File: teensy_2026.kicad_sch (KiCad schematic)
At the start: 12 parts, among them J1 LED, J15 LinAct1, J2 BattManagement, J3 LinearActSaber, J5 LinAct2, U1 RASPBERRY_PI_PICO

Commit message: Merge FIx uo
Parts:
- J15: footprint teensy:4pinJST -> Connector:Tag-Connect_TC2030-IDC-FP_2x03_P1.27mm_Vertical
- J5: footprint teensy:4pinJST -> (none)
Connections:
- net GND: now also J15.4 (Pin_4), J5.4 (Pin_4)
- net LA1_HE1_in: now also J15.1 (Pin_1)
- net LA1_HE2_in: now also J15.2 (Pin_2)
- net LA2_HE1_in: now also J5.1 (Pin_1)
- net LinAct TX: now reaches J3.2 (Pin_2), TP10.1
- new net LA2_HE2_in: J5.2 (Pin_2)
- new net VCC: J15.3 (Pin_3), J5.3 (Pin_3)
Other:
- moved on the sheet: J1, J2, J3, TP10, TP9

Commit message: some small movements
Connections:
- net BattManagement CSn: now also U1.GP1
- net BattManagement TX: now also U1.GP3
- net LA1_HE1_in: now also U1.GP6
- net LA2_HE2_in: now also U1.GP9
- net SCL 0: now also U1.GP19
- no-connect marks 0 -> 17

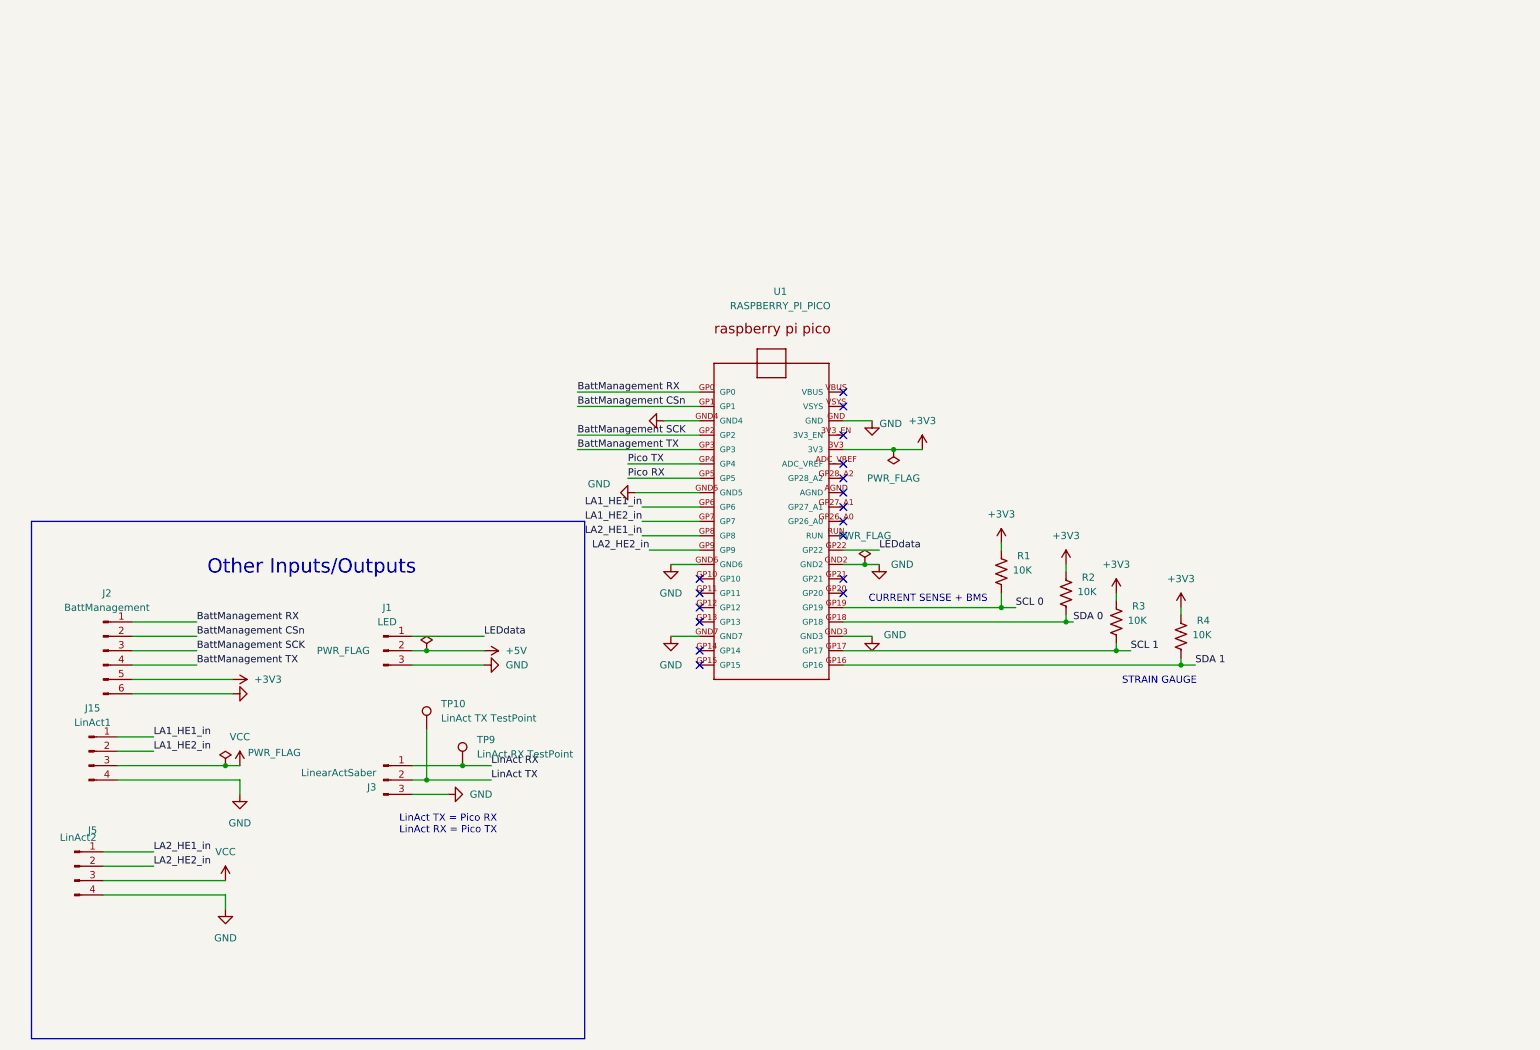
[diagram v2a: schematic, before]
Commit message: Added 3 JSTs for current sense, and 5 JSTs for strain gauge
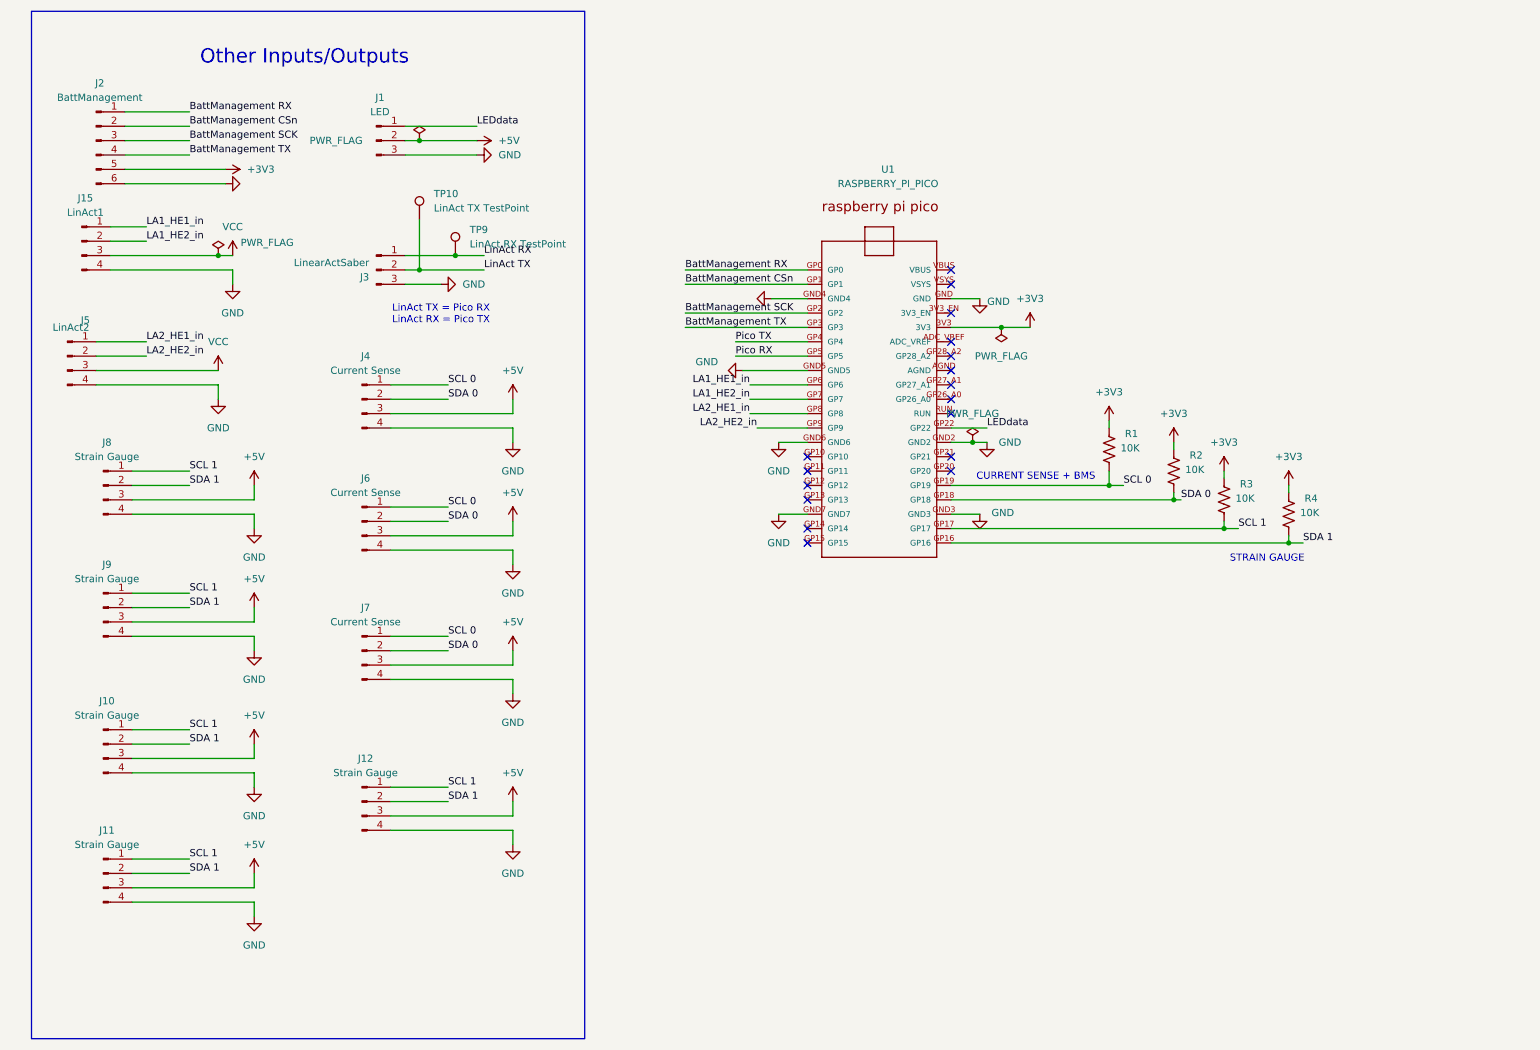
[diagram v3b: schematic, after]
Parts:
- added J10, J11, J12, J8, J9: Strain Gauge, symbol Connector:Conn_01x04_Pin
- added J4, J6, J7: Current Sense, symbol Connector:Conn_01x04_Pin
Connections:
- net +5V: now also J10.3 (Pin_3), J11.3 (Pin_3), J12.3 (Pin_3), J4.3 (Pin_3), J6.3 (Pin_3), J7.3 (Pin_3), J8.3 (Pin_3), J9.3 (Pin_3)
- net GND: now also J10.4 (Pin_4), J11.4 (Pin_4), J12.4 (Pin_4), J4.4 (Pin_4), J6.4 (Pin_4), J7.4 (Pin_4), J8.4 (Pin_4), J9.4 (Pin_4)
- net SCL 0: now also J4.1 (Pin_1), J6.1 (Pin_1), J7.1 (Pin_1)
- net SCL 1: now also J10.1 (Pin_1), J11.1 (Pin_1), J12.1 (Pin_1), J8.1 (Pin_1), J9.1 (Pin_1)
- net SDA 0: now also J4.2 (Pin_2), J6.2 (Pin_2), J7.2 (Pin_2)
- net SDA 1: now also J10.2 (Pin_2), J11.2 (Pin_2), J12.2 (Pin_2), J8.2 (Pin_2), J9.2 (Pin_2)
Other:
- moved on the sheet: J1, J15, J2, J3, J5, R1, R2, R3, R4, TP10, TP9, U1

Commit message: Extra UART
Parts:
- added J13: UART 0 Placeholder, symbol Connector:Conn_01x04_Pin
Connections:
- net +5V: now also J13.3 (Pin_3)
- net GND: now also J13.4 (Pin_4)
- net LA2_HE1_in: now also U1.GP10; no longer U1.GP8
- net LA2_HE2_in: now also U1.GP11; no longer U1.GP9
- new net RX: J13.2 (Pin_2), U1.GP9
- new net TX: J13.1 (Pin_1), U1.GP8
- no-connect marks 17 -> 16
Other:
- moved on the sheet: R1, R2, R3, R4, U1

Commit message: started pcb layout
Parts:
- J1: footprint LED_THT:LED_D5.0mm_IRGrey -> Connector_JST:JST_XH_B3B-XH-A_1x03_P2.50mm_Vertical
- J10, J11, J12, J13, J4, J5, J6, J7, J8, J9: footprint (none) -> Connector_JST:JST_XH_B4B-XH-A_1x04_P2.50mm_Vertical
- J15: footprint Connector:Tag-Connect_TC2030-IDC-FP_2x03_P1.27mm_Vertical -> Connector_JST:JST_XH_B4B-XH-A_1x04_P2.50mm_Vertical
- J2: footprint (none) -> Connector_JST:JST_XH_B6B-XH-A_1x06_P2.50mm_Vertical
- J3: footprint teensy:3pinJST -> Connector_JST:JST_XH_B3B-XH-A_1x03_P2.50mm_Vertical
- R1, R2, R3, R4: footprint Resistor_THT:R_Array_SIP4 -> Resistor_THT:R_Axial_DIN0411_L9.9mm_D3.6mm_P12.70mm_Horizontal
- TP10: footprint Relay_THT:Relay_DPDT_Schrack-RT2-FormC_RM5mm -> Connector_Wire:SolderWire-0.75sqmm_1x01_D1.25mm_OD2.3mm
- TP9: footprint (none) -> Connector_Wire:SolderWire-0.75sqmm_1x01_D1.25mm_OD2.3mm
- U1: footprint RASPBERRY_PI_PICO:RASPBERRY_PI_PICO -> pico:RASPBERRY_PI_PICO
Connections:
- net Pico RX is gone; now on net LinAct RX: U1.GP5
- net Pico TX is gone; now on net LinAct TX: U1.GP4
- net VCC is gone; now on net +5V: J15.3 (Pin_3), J5.3 (Pin_3)
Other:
- note removed: "LinAct TX = Pico RX LinAct RX = Pico TX"
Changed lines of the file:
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@@
 		)
 	)
-	(text "LinAct TX = Pico RX\nLinAct RX = Pico TX \n"
-		(exclude_from_sim no)
-		(at 87.63 68.834 0)
-		(effects
-			(font
-				(size 1.27 1.27)
-			)
-		)
-	)
 	(text "STRAIN GAUGE"
 		(exclude_from_sim no)
@@
 		)
 	)
-	(label "Pico RX"
+	(label "LinAct RX"
 		(at 172.72 57.15 0)
 		(effects
@@
 		)
 	)
-	(label "Pico TX"
+	(label "LinAct TX"
 		(at 172.72 54.61 0)
 		(effects
@@
 			)
 		)
-		(property "Footprint" "Resistor_THT:R_Array_SIP4"
+		(property "Footprint" "Resistor_THT:R_Axial_DIN0411_L9.9mm_D3.6mm_P12.70mm_Horizontal"
 			(at 251.206 77.724 90)
 			(hide yes)
@@
 			)
 		)
-		(property "Footprint" "Resistor_THT:R_Array_SIP4"
+		(property "Footprint" "Resistor_THT:R_Axial_DIN0411_L9.9mm_D3.6mm_P12.70mm_Horizontal"
 			(at 239.776 73.914 90)
 			(hide yes)
@@
 			)
 		)
-		(property "Footprint" ""
+		(property "Footprint" "Connector_JST:JST_XH_B6B-XH-A_1x06_P2.50mm_Vertical"
 			(at 26.67 38.1 0)
 			(hide yes)
@@
 			)
 		)
-		(property "Footprint" "LED_THT:LED_D5.0mm_IRGrey"
+		(property "Footprint" "Connector_JST:JST_XH_B3B-XH-A_1x03_P2.50mm_Vertical"
 			(at 76.2 38.1 0)
 			(hide yes)
@@
 			)
 		)
-		(property "Footprint" "Resistor_THT:R_Array_SIP4"
+		(property "Footprint" "Resistor_THT:R_Axial_DIN0411_L9.9mm_D3.6mm_P12.70mm_Horizontal"
 			(at 260.096 82.804 90)
 			(hide yes)
@@
 			)
 		)
-		(property "Footprint" "Relay_THT:Relay_DPDT_Schrack-RT2-FormC_RM5mm"
+		(property "Footprint" "Connector_Wire:SolderWire-0.75sqmm_1x01_D1.25mm_OD2.3mm"
 			(at 88.9 52.07 0)
 			(hide yes)
@@
 			)
 		)
-		(property "Footprint" ""
+		(property "Footprint" "Connector_JST:JST_XH_B4B-XH-A_1x04_P2.50mm_Vertical"
 			(at 27.94 99.06 0)
 			(hide yes)
@@
 			)
 		)
-		(property "Footprint" ""
+		(property "Footprint" "Connector_JST:JST_XH_B4B-XH-A_1x04_P2.50mm_Vertical"
 			(at 27.94 120.65 0)
 			(hide yes)
@@
 			)
 		)
-		(property "Footprint" ""
+		(property "Footprint" "Connector_JST:JST_XH_B4B-XH-A_1x04_P2.50mm_Vertical"
 			(at 21.59 76.2 0)
 			(hide yes)
@@
 			)
 		)
-		(property "Footprint" "Resistor_THT:R_Array_SIP4"
+		(property "Footprint" "Resistor_THT:R_Axial_DIN0411_L9.9mm_D3.6mm_P12.70mm_Horizontal"
 			(at 271.526 85.344 90)
 			(hide yes)
@@
 			)
 		)
-		(property "Footprint" "teensy:3pinJST"
+		(property "Footprint" "Connector_JST:JST_XH_B3B-XH-A_1x03_P2.50mm_Vertical"
 			(at 76.2 60.96 0)
 			(hide yes)
@@
 		(in_pos_files yes)
 		(dnp no)
-		(fields_autoplaced yes)
 		(property "Reference" "#PWR03"
 			(at 50.8 62.23 0)
@@
 			)
 		)
-		(property "Value" "VCC"
-			(at 50.8 53.34 0)
+		(property "Value" "+5V"
+			(at 48.768 54.102 0)
 			(show_name no)
 			(do_not_autoplace no)
@@
 					(size 1.27 1.27)
 				)
+				(justify left)
 			)
 		)
@@
 			)
 		)
-		(property "Footprint" ""
+		(property "Footprint" "Connector_JST:JST_XH_B4B-XH-A_1x04_P2.50mm_Vertical"
 			(at 27.94 144.78 0)
 			(hide yes)
@@
 			)
 		)
-		(property "Footprint" ""
+		(property "Footprint" "Connector_JST:JST_XH_B4B-XH-A_1x04_P2.50mm_Vertical"
 			(at 73.66 83.82 0)
 			(hide yes)
@@
 			)
 		)
-		(property "Footprint" ""
+		(property "Footprint" "Connector_JST:JST_XH_B4B-XH-A_1x04_P2.50mm_Vertical"
 			(at 120.65 31.75 0)
 			(hide yes)
@@
 			)
 		)
-		(property "Footprint" ""
+		(property "Footprint" "Connector_Wire:SolderWire-0.75sqmm_1x01_D1.25mm_OD2.3mm"
 			(at 95.25 58.42 0)
 			(hide yes)
@@
 			)
 		)
-		(property "Footprint" ""
+		(property "Footprint" "Connector_JST:JST_XH_B4B-XH-A_1x04_P2.50mm_Vertical"
 			(at 73.66 154.94 0)
 			(hide yes)
@@
 		(in_pos_files yes)
 		(dnp no)
-		(fields_autoplaced yes)
 		(property "Reference" "#PWR018"
 			(at 48.26 82.55 0)
@@
 			)
 		)
-		(property "Value" "VCC"
-			(at 48.26 73.66 0)
+		(property "Value" "+5V"
+			(at 47.752 73.914 0)
 			(show_name no)
 			(do_not_autoplace no)
@@
 					(size 1.27 1.27)
 				)
+				(justify left)
 			)
 		)
@@
 			)
 		)
-		(property "Footprint" ""
+		(property "Footprint" "Connector_JST:JST_XH_B4B-XH-A_1x04_P2.50mm_Vertical"
 			(at 73.66 128.27 0)
 			(hide yes)
@@
 			)
 		)
-		(property "Footprint" "RASPBERRY_PI_PICO:RASPBERRY_PI_PICO"
+		(property "Footprint" "pico:RASPBERRY_PI_PICO"
 			(at 195.58 62.23 0)
 			(hide yes)
@@
 			)
 		)
-		(property "Footprint" ""
+		(property "Footprint" "Connector_JST:JST_XH_B4B-XH-A_1x04_P2.50mm_Vertical"
 			(at 73.66 105.41 0)
 			(hide yes)
@@
 			)
 		)
-		(property "Footprint" ""
+		(property "Footprint" "Connector_JST:JST_XH_B4B-XH-A_1x04_P2.50mm_Vertical"
 			(at 27.94 167.64 0)
 			(hide yes)
@@
 			)
 		)
-		(property "Footprint" "Connector:Tag-Connect_TC2030-IDC-FP_2x03_P1.27mm_Vertical"
+		(property "Footprint" "Connector_JST:JST_XH_B4B-XH-A_1x04_P2.50mm_Vertical"
 			(at 24.13 55.88 0)
 			(hide yes)
